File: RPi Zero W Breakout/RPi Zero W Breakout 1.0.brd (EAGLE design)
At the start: 90 x 55 mm, 35 parts, among them J1 35RAPC4BHN2

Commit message: More layer changes
Just moving text between layers for silkscreen. Just realized that RPi 0.3 is saved as 1.0, but oh well.
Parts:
- renumbered PIN1 to J2, U$3 to H1
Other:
- board text added: "L"
- board text added: "R"
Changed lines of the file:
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@@
 <setting verticaltext="up"/>
 </settings>
-<grid distance="10" unitdist="mil" unit="mil" style="lines" multiple="1" display="no" altdistance="1" altunitdist="mm" altunit="mm"/>
+<grid distance="1" unitdist="mm" unit="mm" style="lines" multiple="1" display="no" altdistance="1" altunitdist="mm" altunit="mm"/>
 <layers>
 <layer number="1" name="Top" color="4" fill="1" visible="yes" active="yes"/>
@@
 <wire x1="25" y1="55" x2="25" y2="0" width="0.1524" layer="47"/>
 <wire x1="90" y1="10" x2="0" y2="10" width="0.1524" layer="47"/>
-<wire x1="0" y1="45" x2="10.254" y2="45" width="0.1524" layer="47"/>
 <hole x="10" y="45" drill="2.5"/>
 <hole x="7" y="7" drill="2.5"/>
@@
 <hole x="80" y="45" drill="2.5"/>
 <text x="3.5" y="24" size="1.778" layer="26" rot="MR0">Rf</text>
-<text x="85.5" y="24.5" size="1.778" layer="27">A</text>
-<text x="75.5" y="15" size="1.778" layer="27">B</text>
-<text x="75.5" y="34" size="1.778" layer="27">X</text>
-<text x="66" y="24.5" size="1.778" layer="27">Y</text>
-<text x="51" y="13" size="1.778" layer="27">START</text>
-<text x="41.5" y="13" size="1.778" layer="27">HOME</text>
-<text x="30.5" y="13" size="1.778" layer="27">SELECT</text>
-<text x="16.5" y="43" size="1.778" layer="27">UP</text>
-<text x="22" y="15" size="1.778" layer="27">DOWN</text>
-<text x="5" y="33" size="1.778" layer="27">LEFT</text>
-<text x="31" y="24.5" size="1.778" layer="27">RIGHT</text>
-<text x="59.5" y="3.5" size="1.778" layer="27">RPi ZeroW Breakout
+<text x="85.5" y="24.5" size="1.778" layer="21">A</text>
+<text x="75.5" y="15" size="1.778" layer="21">B</text>
+<text x="75.5" y="34" size="1.778" layer="21">X</text>
+<text x="66" y="24.5" size="1.778" layer="21">Y</text>
+<text x="51" y="13" size="1.778" layer="21">START</text>
+<text x="41.5" y="13" size="1.778" layer="21">HOME</text>
+<text x="30.5" y="13" size="1.778" layer="21">SELECT</text>
+<text x="16.5" y="43" size="1.778" layer="21">UP</text>
+<text x="22" y="15" size="1.778" layer="21">DOWN</text>
+<text x="5" y="33" size="1.778" layer="21">LEFT</text>
+<text x="31" y="24.5" size="1.778" layer="21">RIGHT</text>
+<text x="41.466" y="38.044" size="1.778" layer="21">RPi ZeroW Breakout
 Rev 1 2019 Injoo Moon</text>
-<wire x1="10.254" y1="45" x2="90.254" y2="45" width="0.1524" layer="47"/>
+<wire x1="0" y1="45" x2="90.254" y2="45" width="0.1524" layer="47"/>
+<text x="6" y="50" size="1.778" layer="21">L</text>
+<text x="82" y="50" size="1.778" layer="21">R</text>
 </plain>
 <attributes>
@@
 </autorouter>
 <elements>
-<element name="PIN1" library="con-hirose" library_urn="urn:adsk.eagle:library:152" package="FH12-10S-0.5SH" package3d_urn="urn:adsk.eagle:package:7323/1" value="FH12-10S-0.5SH" x="45" y="34" smashed="yes" rot="R180">
+<element name="J2" library="con-hirose" library_urn="urn:adsk.eagle:library:152" package="FH12-10S-0.5SH" package3d_urn="urn:adsk.eagle:package:7323/1" value="FH12-10S-0.5SH" x="45" y="34" smashed="yes" rot="R180">
 <attribute name="MF" value="" x="19.6" y="68.29" size="1.778" layer="27" rot="R180" display="off"/>
 <attribute name="MPN" value="FH12-10S-0.5SH(55)" x="19.6" y="68.29" size="1.778" layer="27" rot="R180" display="off"/>
@@
 <attribute name="VALUE" x="34.5" y="43" size="0.8128" layer="27" rot="R180"/>
 </element>
-<element name="U$3" library="M22-6340442" package="M22-6340442" value="M22-6340442" x="70.5" y="14" smashed="yes" rot="MR270">
+<element name="H1" library="M22-6340442" package="M22-6340442" value="M22-6340442" x="70.5" y="14" smashed="yes" rot="MR270">
 <attribute name="NAME" x="75" y="11" size="1.016" layer="26" rot="MR180"/>
 </element>
@@
 <signals>
 <signal name="LEDK">
-<contactref element="PIN1" pad="1"/>
+<contactref element="J2" pad="1"/>
 <contactref element="U$1" pad="12"/>
 <wire x1="56.43" y1="48.27" x2="57.658" y2="47.042" width="0.2032" layer="16"/>
@@
 </signal>
 <signal name="MISO">
-<contactref element="PIN1" pad="2"/>
+<contactref element="J2" pad="2"/>
 <contactref element="U$1" pad="21"/>
 <wire x1="43.73" y1="45.73" x2="45.212" y2="44.248" width="0.2032" layer="16"/>
@@
 </signal>
 <signal name="CS">
-<contactref element="PIN1" pad="5"/>
+<contactref element="J2" pad="5"/>
 <contactref element="U$1" pad="24"/>
 <wire x1="45.25" y1="30.75" x2="45.25" y2="29.502" width="0.2032" layer="1"/>
@@
 </signal>
 <signal name="RESET">
-<contactref element="PIN1" pad="8"/>
+<contactref element="J2" pad="8"/>
 <contactref element="U$1" pad="22"/>
 <wire x1="43.73" y1="48.27" x2="44.958" y2="47.042" width="0.2032" layer="1"/>
@@
 <signal name="5V">
 <contactref element="U$2" pad="VDD"/>
-<contactref element="PIN1" pad="9"/>
+<contactref element="J2" pad="9"/>
 <contactref element="U$1" pad="2"/>
 <contactref element="U$1" pad="4"/>
-<contactref element="U$3" pad="P4"/>
+<contactref element="H1" pad="P4"/>
 <wire x1="73.96" y1="16.54" x2="73.96" y2="19.258" width="0.3048" layer="16"/>
 <wire x1="73.96" y1="19.258" x2="73.152" y2="20.066" width="0.3048" layer="16"/>
@@
 </signal>
 <signal name="GND">
-<contactref element="PIN1" pad="10"/>
+<contactref element="J2" pad="10"/>
 <contactref element="C2" pad="2"/>
 <contactref element="R4" pad="1"/>
@@
 <contactref element="U$1" pad="34"/>
 <contactref element="U$1" pad="39"/>
-<contactref element="U$3" pad="P3"/>
+<contactref element="H1" pad="P3"/>
 <polygon width="0.1524" layer="1" rank="6">
 <vertex x="-1" y="-1"/>
@@
 <signal name="MOSI">
 <contactref element="U$1" pad="19"/>
-<contactref element="PIN1" pad="4"/>
+<contactref element="J2" pad="4"/>
 <wire x1="46.27" y1="45.73" x2="46.27" y2="44.746" width="0.2032" layer="16"/>
 <wire x1="46.27" y1="44.746" x2="45.72" y2="44.196" width="0.2032" layer="16"/>
@@
 <signal name="CLK">
 <contactref element="U$1" pad="23"/>
-<contactref element="PIN1" pad="3"/>
+<contactref element="J2" pad="3"/>
 <wire x1="41.19" y1="45.73" x2="41.19" y2="29.676" width="0.2032" layer="16"/>
 <wire x1="41.19" y1="29.676" x2="41.656" y2="29.21" width="0.2032" layer="16"/>
@@
 <signal name="RS/DC">
 <contactref element="U$1" pad="18"/>
-<contactref element="PIN1" pad="7"/>
+<contactref element="J2" pad="7"/>
 <wire x1="44.25" y1="30.75" x2="44.25" y2="32.566" width="0.2032" layer="1"/>
 <wire x1="44.25" y1="32.566" x2="44.958" y2="33.274" width="0.2032" layer="1"/>

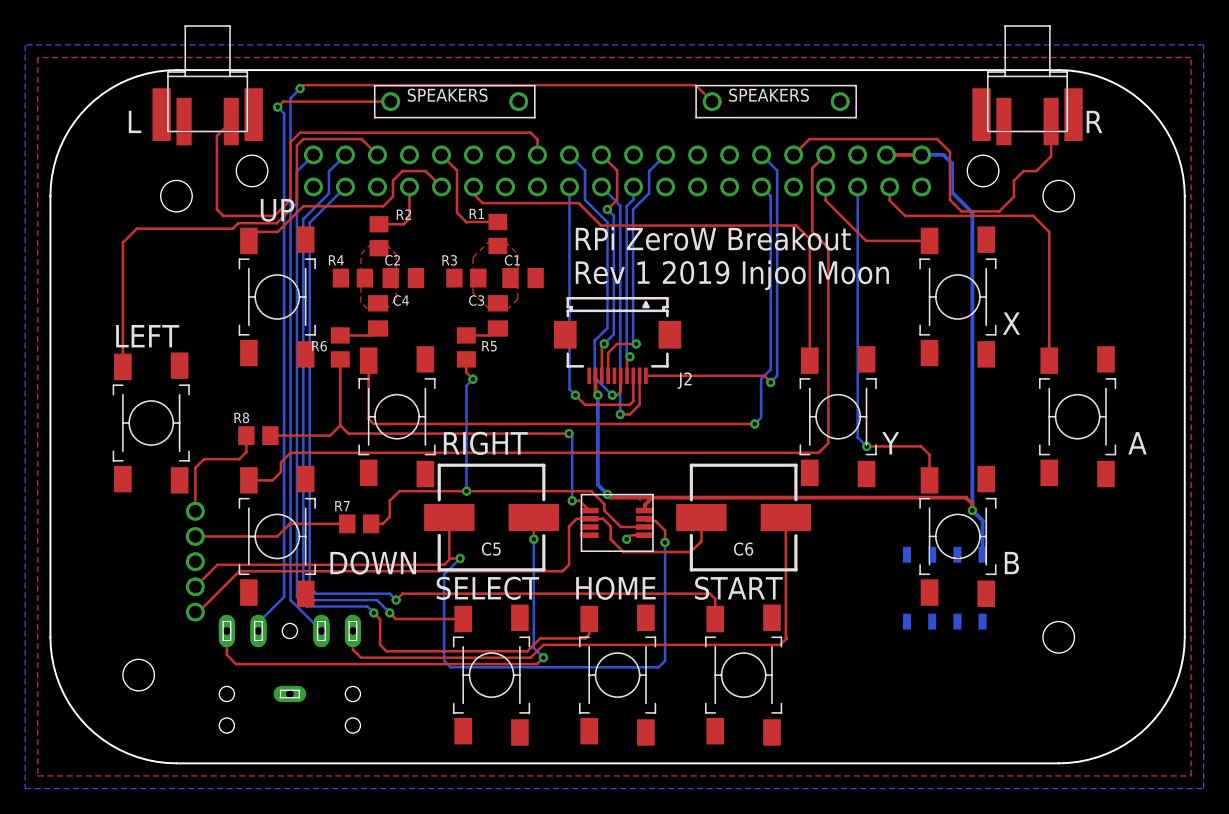
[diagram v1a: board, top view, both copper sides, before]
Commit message: Update
Moved shoulder buttons to LiPoly Management and extended LiPoly Management's dimensions. After looking at the boards in Fusion 360, I decided it would be better to have the shoulder buttons lower, rather than up high on RPi Zero Breakout. Rereouted LiPoly due to this.
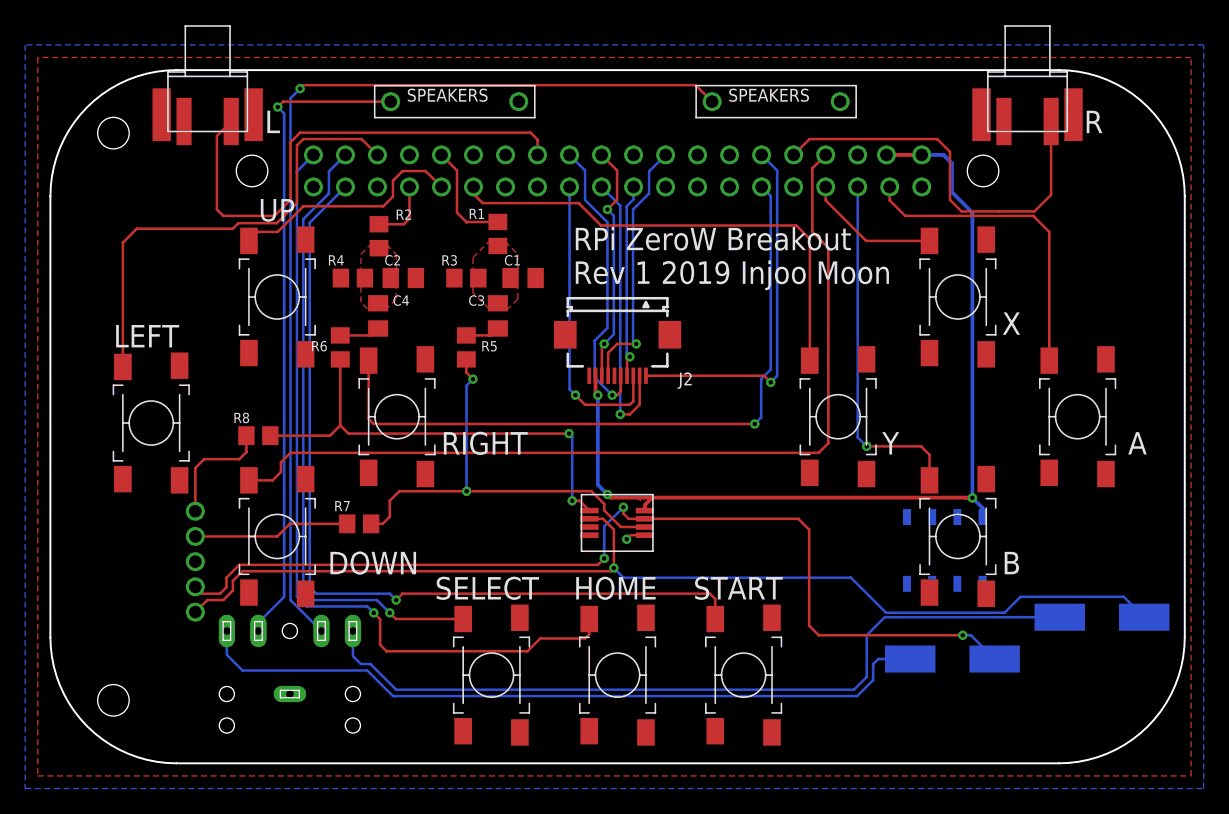
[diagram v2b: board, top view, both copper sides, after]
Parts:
- moved C5 38.3 mm to (71.6, 8.28), flipped to the bottom
- moved C6 29.5 mm to (83.4, 11.6), flipped to the bottom
- moved H1 3.00 mm to (70.5, 17.0)
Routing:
- net N$8: track 49.1 -> 85.2 mm, vias 0 -> 1
- net N$10: track 39.0 -> 59.4 mm, vias 2 -> 0
- net N$11: track 46.4 -> 63.5 mm
- net N$9: track 64.2 -> 78.2 mm, vias 2 -> 3
- net 5V: track 78.4 -> 74.7 mm
- net R: track 30.9 -> 31.9 mm
